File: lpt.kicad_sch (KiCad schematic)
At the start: 15 parts, among them J6 DB25 FEMALE, U2 74HC245, U3 74HC245, U4 ACSL-6310, U5 ACSL-6310

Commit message: checkpoint
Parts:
- added JP9: GND_ISO, Connector_PinHeader_2.54mm:PinHeader_1x02_P2.54mm_Vertical, symbol Jumper:Jumper_2_Bridged
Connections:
- net GND1: now also JP9.2 (B); no longer JP3.2 (B)
- net GNDA: now also JP9.1 (A)
- net P14_IN: now also U2.9 (A7); no longer U2.3 (A1)
- net P14_OUT: now also U2.11 (B7); no longer U2.17 (B1)
- net P16_IN: now also U3.6 (A4); no longer U2.2 (A0)
- net P16_OUT: now also U3.14 (B4); no longer U2.18 (B0)
- net P17_OUT: now also U3.13 (B5); no longer U3.17 (B1)
- net P1_IN: now also U2.2 (A0); no longer U3.2 (A0)
- net P1_OUT: now also U2.18 (B0); no longer U3.18 (B0)
- net P2_IN: now also U2.3 (A1); no longer U2.4 (A2)
- net P2_OUT: now also U2.17 (B1); no longer U2.16 (B2)
- net P3_IN: now also U2.4 (A2); no longer U2.5 (A3)
- net P3_OUT: now also U2.16 (B2); no longer U2.15 (B3)
- net P4_IN: now also U2.5 (A3); no longer U2.6 (A4)
- net P4_OUT: now also U2.15 (B3); no longer U2.14 (B4)
- net P5_IN: now also U2.6 (A4); no longer U2.7 (A5)
- net P5_OUT: now also U2.14 (B4); no longer U2.13 (B5)
- net P6_IN: now also U2.7 (A5); no longer U2.8 (A6)
- net P6_OUT: now also U2.13 (B5); no longer U2.12 (B6)
- net P7_IN: now also U2.8 (A6); no longer U2.9 (A7)
- net P7_OUT: now also U2.12 (B6); no longer U2.11 (B7)
- net P8_OUT: now also U3.12 (B6); no longer U3.16 (B2)
- net P9_OUT: now also U3.11 (B7); no longer U3.15 (B3)
- new net GND: JP3.2 (B)
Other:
- moved on the sheet: JP3, R13

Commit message: v4 MILESTONE
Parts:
- removed JP9: GND_ISO, Connector_PinHeader_2.54mm:PinHeader_1x02_P2.54mm_Vertical, symbol Jumper:Jumper_2_Bridged
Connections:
- net GNDA: no longer U4.16 (GND), U4.9 (GND), U5.16 (GND), U5.9 (GND)
- net P14_IN: now also U2.8 (A6); no longer U2.9 (A7)
- net P14_OUT: now also U2.12 (B6); no longer U2.11 (B7)
- net P16_OUT: now also U3.15 (B3); no longer U3.14 (B4)
- net P17_OUT: now also U3.14 (B4); no longer U3.13 (B5)
- net P1_IN: now also U3.9 (A7); no longer U2.2 (A0)
- net P1_OUT: now also U3.11 (B7); no longer U2.18 (B0)
- net P2_IN: now also U2.2 (A0); no longer U2.3 (A1)
- net P2_OUT: now also U2.18 (B0); no longer U2.17 (B1)
- net P3_IN: now also U2.3 (A1); no longer U2.4 (A2)
- net P3_OUT: now also U2.17 (B1); no longer U2.16 (B2)
- net P4_IN: now also U2.4 (A2); no longer U2.5 (A3)
- net P4_OUT: now also U2.16 (B2); no longer U2.15 (B3)
- net P5_IN: now also U2.5 (A3); no longer U2.6 (A4)
- net P5_OUT: now also U2.15 (B3); no longer U2.14 (B4)
- net P6_IN: now also U2.6 (A4); no longer U2.7 (A5)
- net P6_OUT: now also U2.14 (B4); no longer U2.13 (B5)
- net P7_IN: now also U2.7 (A5); no longer U2.8 (A6)
- net P7_OUT: now also U2.13 (B5); no longer U2.12 (B6)
- net P8_OUT: now also U3.13 (B5); no longer U3.12 (B6)
- net P9_OUT: now also U3.12 (B6); no longer U3.11 (B7)
- net +5V renamed +5VA
- new net GND2: U4.16 (GND), U4.9 (GND), U5.16 (GND), U5.9 (GND)
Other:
- moved on the sheet: R13

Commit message: wip
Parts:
- R13: Marking (none) -> 01E
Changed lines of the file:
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@@
       (effects (font (size 1.27 1.27)) hide)
     )
+    (property "Marking" "01E" (id 11) (at 74.93 109.22 90))
     (pin "1")
     (pin "2")

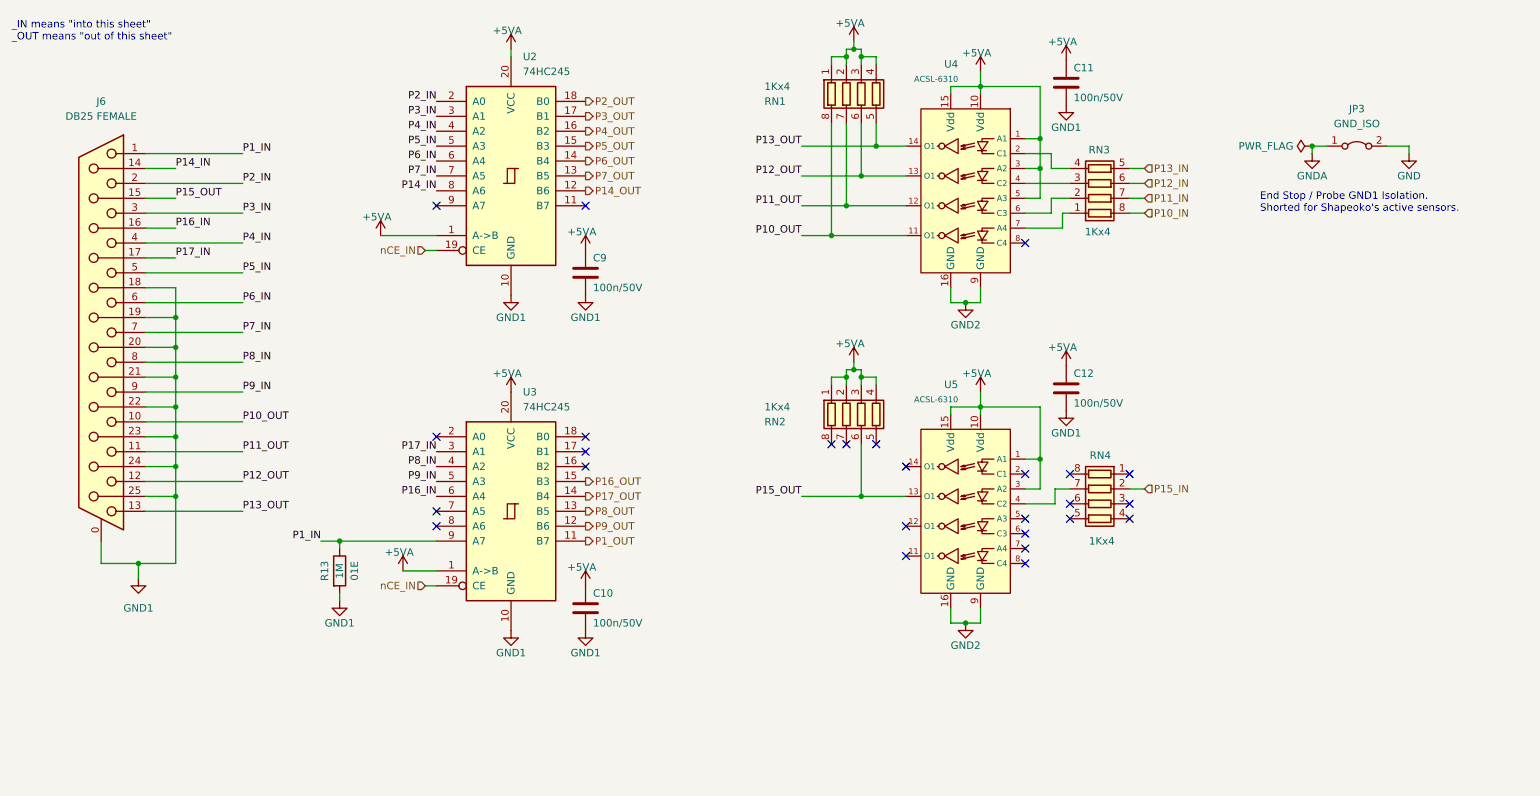
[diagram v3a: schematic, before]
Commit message: Optical isolator input current (10mA not 3mA) and wiring error fixed.
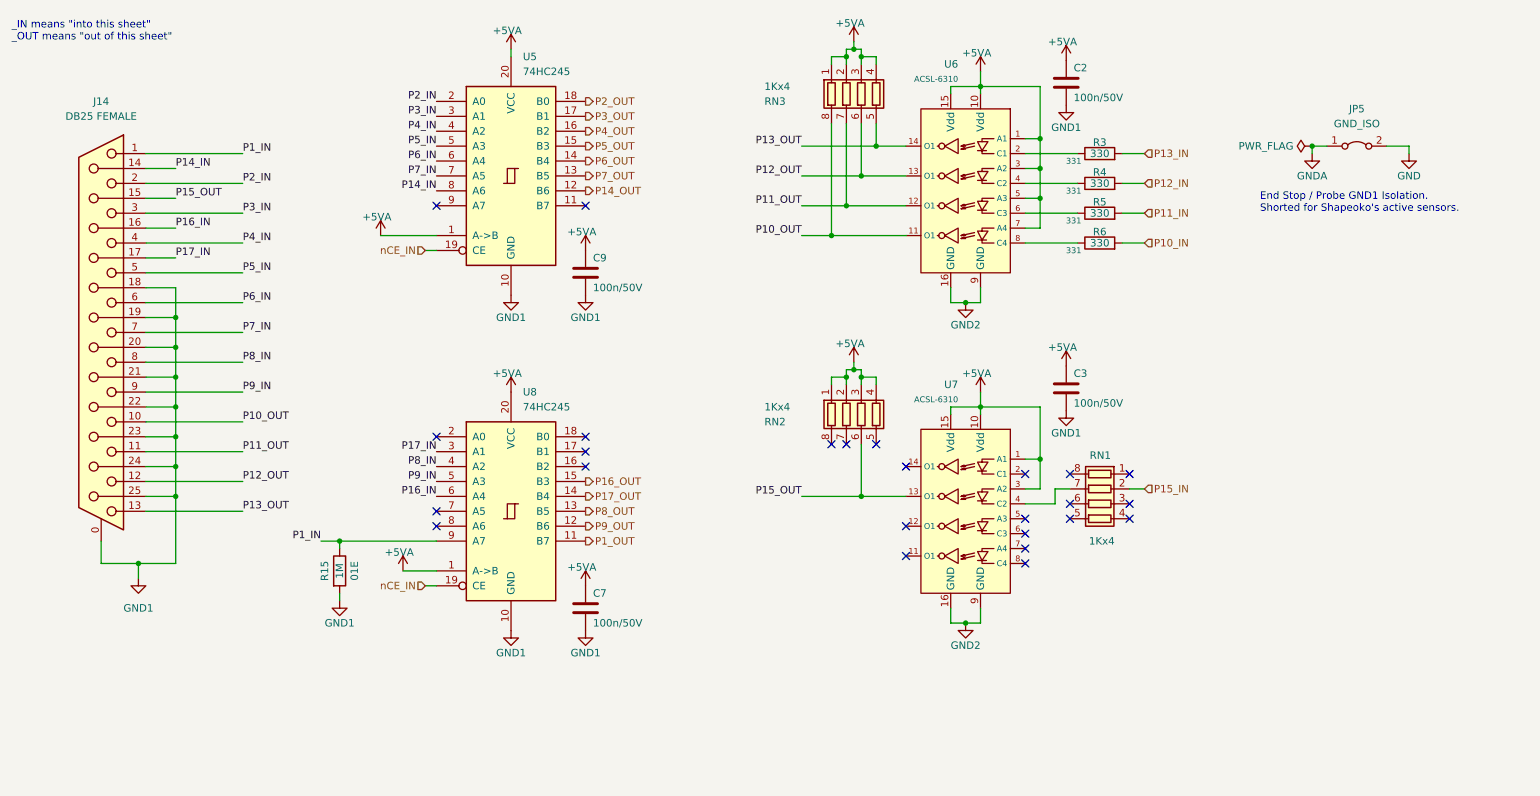
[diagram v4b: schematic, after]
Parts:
- removed RN3: 1Kx4, Resistor_SMD:R_Array_Convex_4x0603, symbol Device:R_Pack04
- added R3, R4, R5, R6: 330, Resistor_SMD:R_0603_1608Metric, symbol Device:R
- renumbered C11 to C2, C12 to C3, C10 to C7, J6 to J14, JP3 to JP5, R13 to R15, RN4 to RN1, RN1 to RN3, U2 to U5, U4 to U6, U5 to U7, U3 to U8
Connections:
- net +5VA: now also U6.7 (A4)
- net P10_IN: now also R6.2
- net P11_IN: now also R5.2
- net P12_IN: now also R4.2
- net P13_IN: now also R3.2
- net at U6.6 (C3): now also R5.1
- net at U6.4 (C2): now also R4.1
- net at U6.2 (C1): now also R3.1
- net at U6.8 (C4): now also R6.1
- no-connect marks 26 -> 25

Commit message: Multiple flaws resolved
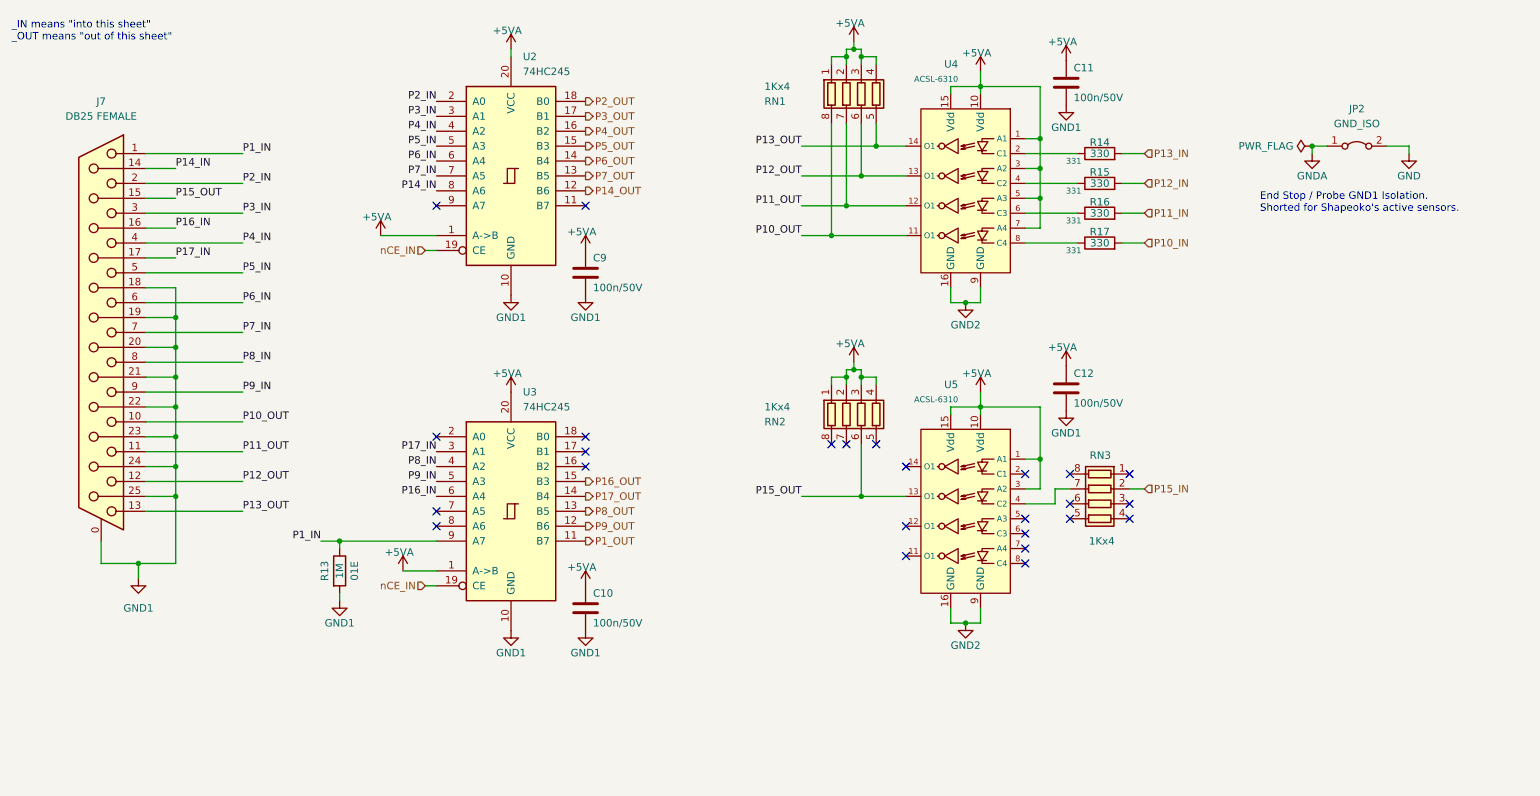
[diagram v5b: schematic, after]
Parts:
- renumbered C7 to C10, C2 to C11, C3 to C12, J14 to J7, JP5 to JP2, R15 to R13, R3 to R14, R4 to R15, R5 to R16, R6 to R17, RN3 to RN1, RN1 to RN3, U5 to U2, U8 to U3, U6 to U4, U7 to U5

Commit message: Oh ... just a few more fuckups fixed
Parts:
- added NT1: NetTie_2, -Project:NetTie-2_SMD_Pad0.3mm, symbol Device:NetTie_2
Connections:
- net P16_IN: now also U3.2 (A0); no longer U3.6 (A4)
- net P16_OUT: now also U3.18 (B0); no longer U3.15 (B3)
- net P17_OUT: now also U3.17 (B1); no longer U3.14 (B4)
- net P1_IN: now also NT1.1; no longer U3.9 (A7)
- net P1_OUT: now also NT1.2; no longer U3.11 (B7)
- net P8_OUT: now also U3.16 (B2); no longer U3.13 (B5)
- net P9_OUT: now also U3.15 (B3); no longer U3.12 (B6)
- no-connect marks 25 -> 27
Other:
- note added: "open collector outputs"
- moved on the sheet: R13

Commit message: wip
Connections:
- net GND1: now also U2.9 (A7), U3.6 (A4), U3.7 (A5), U3.8 (A6), U3.9 (A7)
- no-connect marks 27 -> 22
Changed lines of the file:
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@@
   (junction (at 69.215 130.175) (diameter 0) (color 0 0 0 0)
   )
+  (junction (at 88.9 99.06) (diameter 0) (color 0 0 0 0)
+  )
   (junction (at 181.61 26.67) (diameter 0) (color 0 0 0 0)
   )
@@
   (junction (at 44.45 81.28) (diameter 0) (color 0 0 0 0)
   )
+  (junction (at 88.9 101.6) (diameter 0) (color 0 0 0 0)
+  )
   (junction (at 158.75 21.59) (diameter 0) (color 0 0 0 0)
   )
@@
   )
   (junction (at 238.125 36.83) (diameter 0) (color 0 0 0 0)
+  )
+  (junction (at 88.9 96.52) (diameter 0) (color 0 0 0 0)
   )
   (junction (at 44.45 66.04) (diameter 0) (color 0 0 0 0)
@@
   (no_connect (at 168.91 106.68))
   (no_connect (at 189.23 92.71))
-  (no_connect (at 88.9 46.99))
   (no_connect (at 189.23 100.33))
   (no_connect (at 189.23 102.87))
@@
   (no_connect (at 114.3 99.06))
   (no_connect (at 207.01 92.71))
-  (no_connect (at 88.9 96.52))
-  (no_connect (at 88.9 99.06))
   (no_connect (at 114.3 104.14))
   (no_connect (at 189.23 105.41))
   (no_connect (at 189.23 107.95))
-  (no_connect (at 88.9 104.14))
   (no_connect (at 158.75 87.63))
   (no_connect (at 196.85 92.71))
@@
   (no_connect (at 114.3 96.52))
   (no_connect (at 114.3 101.6))
-  (no_connect (at 88.9 101.6))
   (no_connect (at 168.91 101.6))
   (no_connect (at 163.83 87.63))
@@
     (stroke (width 0) (type default) (color 0 0 0 0))
   )
+  (wire (pts (xy 88.9 104.14) (xy 88.9 101.6))
+    (stroke (width 0) (type default) (color 0 0 0 0))
+  )
   (wire (pts (xy 189.23 95.25) (xy 191.77 95.25))
     (stroke (width 0) (type default) (color 0 0 0 0))
@@
     (stroke (width 0) (type default) (color 0 0 0 0))
   )
+  (wire (pts (xy 88.9 99.06) (xy 88.9 101.6))
+    (stroke (width 0) (type default) (color 0 0 0 0))
+  )
   (wire (pts (xy 205.74 48.26) (xy 209.55 48.26))
     (stroke (width 0) (type default) (color 0 0 0 0))
@@
     (stroke (width 0) (type default) (color 0 0 0 0))
   )
+  (wire (pts (xy 83.185 96.52) (xy 88.9 96.52))
+    (stroke (width 0) (type default) (color 0 0 0 0))
+  )
   (wire (pts (xy 39.37 38.1) (xy 55.88 38.1))
     (stroke (width 0) (type default) (color 0 0 0 0))
@@
     (stroke (width 0) (type default) (color 0 0 0 0))
   )
+  (wire (pts (xy 88.9 46.99) (xy 86.36 46.99))
+    (stroke (width 0) (type default) (color 0 0 0 0))
+  )
   (wire (pts (xy 44.45 66.04) (xy 44.45 71.12))
     (stroke (width 0) (type default) (color 0 0 0 0))
@@
   )
   (wire (pts (xy 163.83 77.47) (xy 163.83 76.2))
+    (stroke (width 0) (type default) (color 0 0 0 0))
+  )
+  (wire (pts (xy 88.9 96.52) (xy 88.9 99.06))
     (stroke (width 0) (type default) (color 0 0 0 0))
   )
@@
       (effects (font (size 1.27 1.27)) (justify left))
     )
-    (property "Footprint" "Package_SO:SOIC-20W_7.5x12.8mm_P1.27mm" (id 2) (at 101.6 99.06 0)
-      (effects (font (size 1.27 1.27)) hide)
-    )
-    (property "Datasheet" "http://www.ti.com/lit/gpn/sn74HC245" (id 3) (at 101.6 99.06 0)
+    (property "Footprint" "Package_SO:SOIC-20W_7.5x12.8mm_P1.27mm" (id 2) (at 124.46 116.84 0)
+      (effects (font (size 1.27 1.27)) hide)
+    )
+    (property "Datasheet" "http://www.ti.com/lit/gpn/sn74HC245" (id 3) (at 129.54 114.935 0)
       (effects (font (size 1.27 1.27)) hide)
     )
@@
       (effects (font (size 1.27 1.27)) hide)
     )
-    (property "E14PART" "1013973" (id 6) (at 101.6 99.06 0)
-      (effects (font (size 1.27 1.27)) hide)
-    )
-    (property "JLCMFR#" "74HC245D,653" (id 7) (at 101.6 99.06 0)
+    (property "E14PART" "1013973" (id 6) (at 122.555 109.22 0)
+      (effects (font (size 1.27 1.27)) hide)
+    )
+    (property "JLCMFR#" "74HC245D,653" (id 7) (at 122.555 111.125 0)
       (effects (font (size 1.27 1.27)) hide)
     )
@@
       (effects (font (size 1.27 1.27)) hide)
     )
-    (property "JLCPART" "C5625" (id 9) (at 101.6 99.06 0)
-      (effects (font (size 1.27 1.27)) hide)
-    )
-    (property "E14MFR#" "MM74HC245AWM" (id 10) (at 101.6 99.06 0)
+    (property "JLCPART" "C5625" (id 9) (at 123.825 107.315 0)
+      (effects (font (size 1.27 1.27)) hide)
+    )
+    (property "E14MFR#" "MM74HC245AWM" (id 10) (at 122.555 113.03 0)
       (effects (font (size 1.27 1.27)) hide)
     )
@@
     (pin "8")
   )
-  (symbol (lib_id "74xx:74HC245") (at 101.6 41.91 0) (unit 1)
+  (symbol (lib_name "74HC245_1") (lib_id "74xx:74HC245") (at 101.6 41.91 0) (unit 1)
     (in_bom yes) (on_board yes) (fields_autoplaced)
     (property "Reference" "U2" (id 0) (at 103.6194 21.59 0)
@@
     (pin "1")
   )
+  (symbol (lib_id "power:GND1") (at 86.36 46.99 0) (unit 1)
+    (in_bom yes) (on_board yes)
+    (property "Reference" "#PWR0104" (id 0) (at 86.36 53.34 0)
+      (effects (font (size 1.27 1.27)) hide)
+    )
+    (property "Value" "GND1" (id 1) (at 86.36 50.8 0))
+    (property "Footprint" "" (id 2) (at 86.36 46.99 0)
+      (effects (font (size 1.27 1.27)) hide)
+    )
+    (property "Datasheet" "" (id 3) (at 86.36 46.99 0)
+      (effects (font (size 1.27 1.27)) hide)
+    )
+    (pin "1")
+  )
   (symbol (lib_id "power:GND2") (at 247.015 85.09 90) (unit 1)
     (in_bom yes) (on_board yes)
@@
       (effects (font (size 1.27 1.27)) hide)
     )
+    (pin "1")
+  )
+  (symbol (lib_id "power:GND1") (at 83.185 96.52 0) (unit 1)
+    (in_bom yes) (on_board yes)
+    (property "Reference" "#PWR0105" (id 0) (at 83.185 102.87 0)
+      (effects (font (size 1.27 1.27)) hide)
+    )
+    (property "Value" "GND1" (id 1) (at 83.185 100.33 0))
+    (property "Footprint" "" (id 2) (at 83.185 96.52 0)
+      (effects (font (size 1.27 1.27)) hide)
+    )
+    (property "Datasheet" "" (id 3) (at 83.185 96.52 0)
+      (effects (font (size 1.27 1.27)) hide)
+    )
